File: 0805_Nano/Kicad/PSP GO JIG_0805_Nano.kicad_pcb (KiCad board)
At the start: 2 copper layers, 20.1 x 14 mm, 12 parts

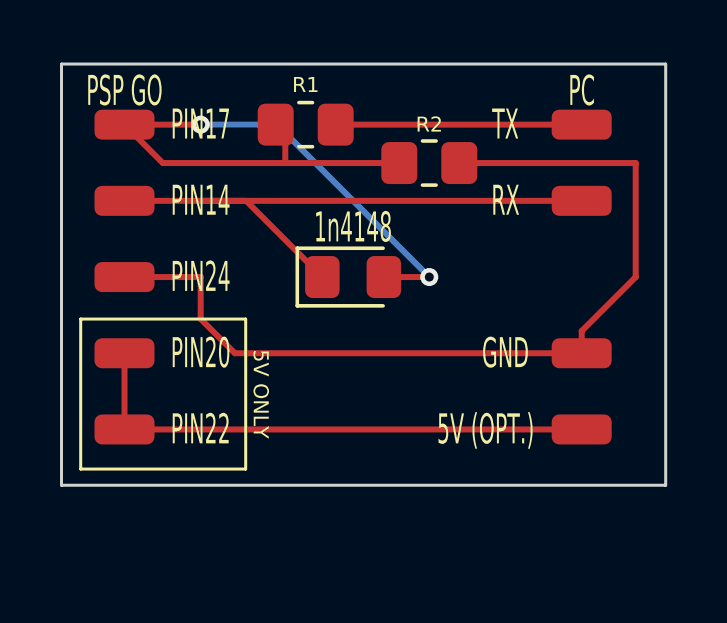
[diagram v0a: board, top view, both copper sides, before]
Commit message: fixed issues pertaining to k-line schematics
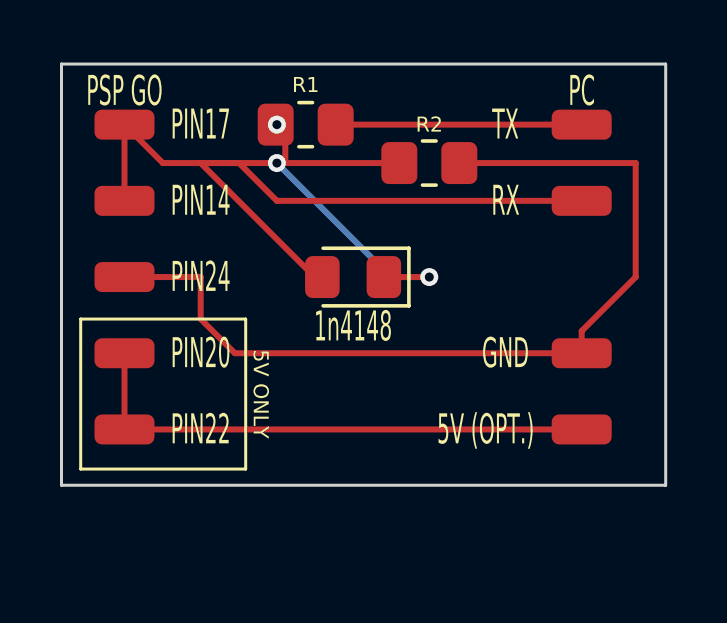
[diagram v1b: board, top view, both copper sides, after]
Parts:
- turned 1n4148 to 180 degrees
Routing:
- net (no net): track 101.3 -> 96.7 mm, vias 2 -> 3
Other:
- board text added: "PSP GO JIG 0805 Rev 1.1 by Mathieulh"
- board text removed: "PSP GO JIG 0805 Rev 1.0 by Mathieulh"
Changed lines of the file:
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@@
   )
   (footprint "Diode_SMD:D_0805_2012Metric_Pad1.15x1.40mm_HandSolder" (layer "F.Cu")
-    (at 68.58 38.1)
+    (at 68.58 38.1 180)
     (descr "Diode SMD 0805 (2012 Metric), square (rectangular) end terminal, IPC_7351 nominal, (Body size source: https://docs.google.com/spreadsheets/d/1BsfQQcO9C6DZCsRaXUlFlo91Tg2WpOkGARC1WS5S8t0/edit?usp=sharing), generated with kicad-footprint-generator")
     (tags "diode handsolder")
@@
     (fp_line (start 1 0.6) (end 1 -0.6)
       (stroke (width 0.1) (type solid)) (layer "F.Fab"))
-    (pad "1" smd roundrect (at -1.025 0) (size 1.15 1.4) (layers "F.Cu" "F.Paste" "F.Mask") (roundrect_rratio 0.217391))
-    (pad "2" smd roundrect (at 1.025 0) (size 1.15 1.4) (layers "F.Cu" "F.Paste" "F.Mask") (roundrect_rratio 0.217391))
+    (pad "1" smd roundrect (at -1.025 0 180) (size 1.15 1.4) (layers "F.Cu" "F.Paste" "F.Mask") (roundrect_rratio 0.217391))
+    (pad "2" smd roundrect (at 1.025 0 180) (size 1.15 1.4) (layers "F.Cu" "F.Paste" "F.Mask") (roundrect_rratio 0.217391))
     (model "${KICAD6_3DMODEL_DIR}/Diode_SMD.3dshapes/D_0805_2012Metric.wrl"
       (offset (xyz 0 0 0))
@@
     (effects (font (size 0.7 0.7) (thickness 0.125) bold) (justify left bottom mirror))
   )
-  (gr_text "PSP GO JIG 0805 Rev 1.0 by Mathieulh" (at 73.66 32.37) (layer "B.SilkS")
+  (gr_text "PSP GO JIG 0805 Rev 1.1 by Mathieulh" (at 73.66 32.37) (layer "B.SilkS")
     (effects (font (size 0.7 0.5) (thickness 0.1) bold) (justify left bottom mirror))
   )
@@
     (effects (font (size 1 0.5) (thickness 0.15)))
   )
-  (segment (start 66.32 33.34) (end 66 33.02) (width 0.2) (layer "F.Cu") (net 0))
+  (segment (start 66.32 34.3) (end 63.5 34.3) (width 0.2) (layer "F.Cu") (net 0))
+  (segment (start 66.32 33.34) (end 66.04 33.06) (width 0.2) (layer "F.Cu") (net 0))
   (segment (start 62.24 34.3) (end 60.96 33.02) (width 0.2) (layer "F.Cu") (net 0))
-  (segment (start 66.32 34.3) (end 62.24 34.3) (width 0.2) (layer "F.Cu") (net 0))
+  (segment (start 63.5 34.3) (end 62.24 34.3) (width 0.2) (layer "F.Cu") (net 0))
   (segment (start 60.96 38.1) (end 63.5 38.1) (width 0.2) (layer "F.Cu") (net 0))
+  (segment (start 66.04 33.02) (end 66 33.02) (width 0.2) (layer "F.Cu") (net 0))
+  (segment (start 66.04 33.06) (end 66.04 33.02) (width 0.2) (layer "F.Cu") (net 0))
   (segment (start 78 38.1) (end 76.2 39.9) (width 0.2) (layer "F.Cu") (net 0))
   (segment (start 64.64 40.64) (end 76.2 40.64) (width 0.2) (layer "F.Cu") (net 0))
-  (segment (start 60.96 33.02) (end 63.5 33.02) (width 0.2) (layer "F.Cu") (net 0))
   (segment (start 63.5 38.1) (end 63.5 39.5) (width 0.2) (layer "F.Cu") (net 0))
   (segment (start 78 34.3) (end 78 38.1) (width 0.2) (layer "F.Cu") (net 0))
+  (segment (start 60.96 33.02) (end 60.96 35.56) (width 0.2) (layer "F.Cu") (net 0))
+  (segment (start 66 33.02) (end 66 33.02) (width 0.2) (layer "F.Cu") (net 0))
   (segment (start 66.32 34.3) (end 66.32 33.34) (width 0.2) (layer "F.Cu") (net 0))
+  (segment (start 67.3 38.1) (end 63.5 34.3) (width 0.2) (layer "F.Cu") (net 0))
   (segment (start 63.5 39.5) (end 64.64 40.64) (width 0.2) (layer "F.Cu") (net 0))
   (segment (start 60.96 43.18) (end 60.96 40.64) (width 0.2) (layer "F.Cu") (net 0))
   (segment (start 70.12 34.3) (end 66.32 34.3) (width 0.2) (layer "F.Cu") (net 0))
+  (segment (start 66.04 35.56) (end 64.78 34.3) (width 0.2) (layer "F.Cu") (net 0))
+  (segment (start 67.555 38.1) (end 67.3 38.1) (width 0) (layer "F.Cu") (net 0))
+  (segment (start 64.78 34.3) (end 63.5 34.3) (width 0.2) (layer "F.Cu") (net 0))
   (segment (start 72.12 34.3) (end 78 34.3) (width 0.2) (layer "F.Cu") (net 0))
-  (segment (start 63.5 35.56) (end 76.2 35.56) (width 0.2) (layer "F.Cu") (net 0))
   (segment (start 76.2 39.9) (end 76.2 40.64) (width 0.2) (layer "F.Cu") (net 0))
+  (segment (start 66.04 35.56) (end 76.2 35.56) (width 0.2) (layer "F.Cu") (net 0))
   (segment (start 68 33.02) (end 76.2 33.02) (width 0.2) (layer "F.Cu") (net 0))
-  (segment (start 67.555 38.1) (end 65.015 35.56) (width 0.2) (layer "F.Cu") (net 0))
-  (segment (start 65.015 35.56) (end 63.5 35.56) (width 0.2) (layer "F.Cu") (net 0))
-  (segment (start 60.96 35.56) (end 63.5 35.56) (width 0.2) (layer "F.Cu") (net 0))
   (segment (start 71.12 38.1) (end 69.605 38.1) (width 0.2) (layer "F.Cu") (net 0))
   (segment (start 60.96 43.18) (end 76.2 43.18) (width 0.2) (layer "F.Cu") (net 0))
+  (via (at 66.04 33.02) (size 0.6) (drill 0.3) (layers "F.Cu" "B.Cu") (net 0))
   (via (at 71.12 38.1) (size 0.6) (drill 0.3) (layers "F.Cu" "B.Cu") (net 0))
-  (via (at 63.5 33.02) (size 0.6) (drill 0.3) (layers "F.Cu" "B.Cu") (net 0))
-  (segment (start 63.5 33.02) (end 66.04 33.02) (width 0.2) (layer "B.Cu") (net 0))
-  (segment (start 66.04 33.02) (end 71.12 38.1) (width 0.2) (layer "B.Cu") (net 0))
+  (via (at 66.04 34.3) (size 0.6) (drill 0.3) (layers "F.Cu" "B.Cu") (net 0))
+  (segment (start 69.84 38.1) (end 71.12 38.1) (width 0.2) (layer "B.Cu") (net 0))
+  (segment (start 66.04 34.3) (end 69.84 38.1) (width 0.2) (layer "B.Cu") (net 0))
 )

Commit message: Fixed PIN24
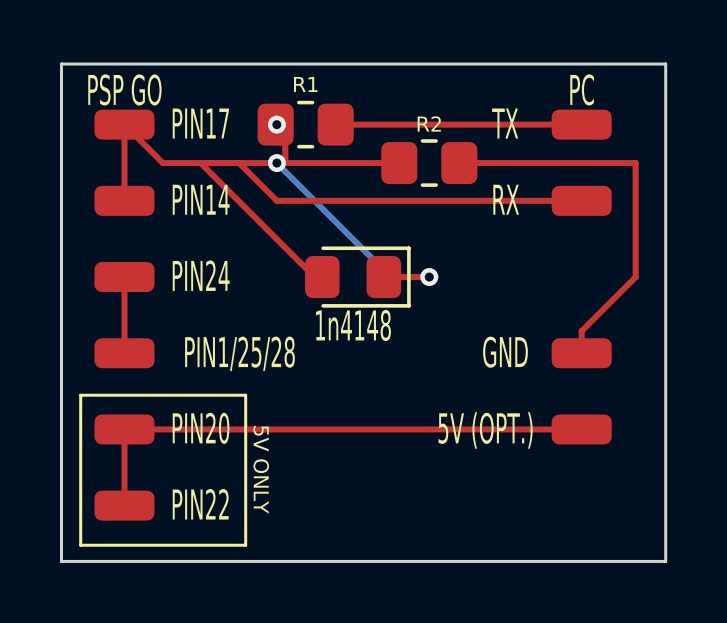
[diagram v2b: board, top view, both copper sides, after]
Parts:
- added REF**: SolderWirePad_1x01_SMD_1x2mm, Connector_Wire:SolderWirePad_1x01_SMD_1x2mm, F.Cu at (61.0, 40.6)
- moved REF** 2.54 mm to (61.0, 45.7)
- moved REF** 2.54 mm to (61.0, 43.2)
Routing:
- net (no net): track 96.7 -> 66.9 mm
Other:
- board size 20.1 x 14 mm -> 20.1 x 16.6 mm
- board text added: "PIN1/25/28"

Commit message: Cleanup + fix GND
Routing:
- net (no net): vias 3 -> 2
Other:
- board text added: "PSP GO JIG 0805 Rev 1.2 by Mathieulh"
- board text removed: "PSP GO JIG 0805 Rev 1.1 by Mathieulh"
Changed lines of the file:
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@@
   (gr_line (start 60.96 43.18) (end 76.2 43.18)
+    (stroke (width 0.2) (type default)) (layer "F.Cu"))
+  (gr_line (start 76.2 40.64) (end 60.96 40.64)
     (stroke (width 0.2) (type default)) (layer "F.Cu"))
   (gr_rect (start 69.46 36.19) (end 76.2 40.01)
@@
     (effects (font (size 0.7 0.7) (thickness 0.125) bold) (justify left bottom mirror))
   )
-  (gr_text "PSP GO JIG 0805 Rev 1.1 by Mathieulh" (at 73.66 32.37) (layer "B.SilkS")
+  (gr_text "PSP GO JIG 0805 Rev 1.2 by Mathieulh" (at 73.66 32.37) (layer "B.SilkS")
     (effects (font (size 0.7 0.5) (thickness 0.1) bold) (justify left bottom mirror))
   )
@@
   (segment (start 71.12 38.1) (end 69.605 38.1) (width 0.2) (layer "F.Cu") (net 0))
   (segment (start 60.96 38.1) (end 60.96 40.64) (width 0.2) (layer "F.Cu") (net 0))
-  (via (at 66.04 33.02) (size 0.6) (drill 0.3) (layers "F.Cu" "B.Cu") (net 0))
   (via (at 71.12 38.1) (size 0.6) (drill 0.3) (layers "F.Cu" "B.Cu") (net 0))
   (via (at 66.04 34.3) (size 0.6) (drill 0.3) (layers "F.Cu" "B.Cu") (net 0))

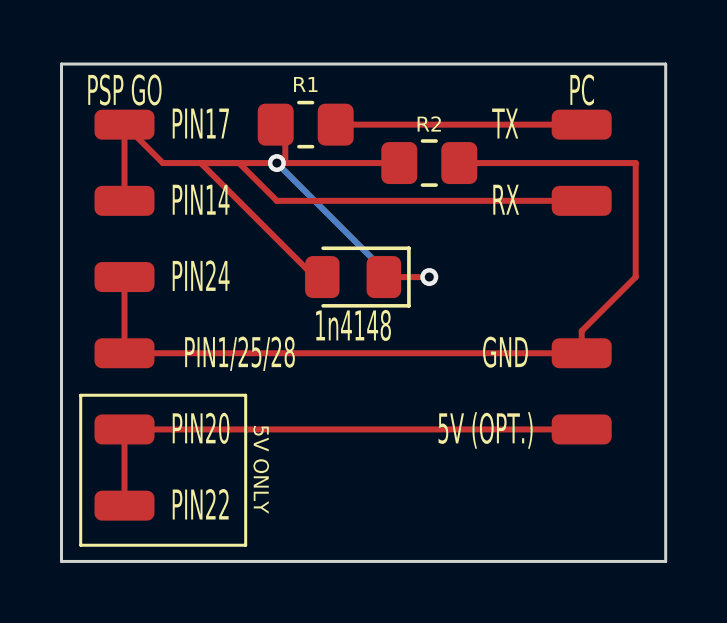
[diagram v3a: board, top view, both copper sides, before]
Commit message: Fixed design issue on nano board
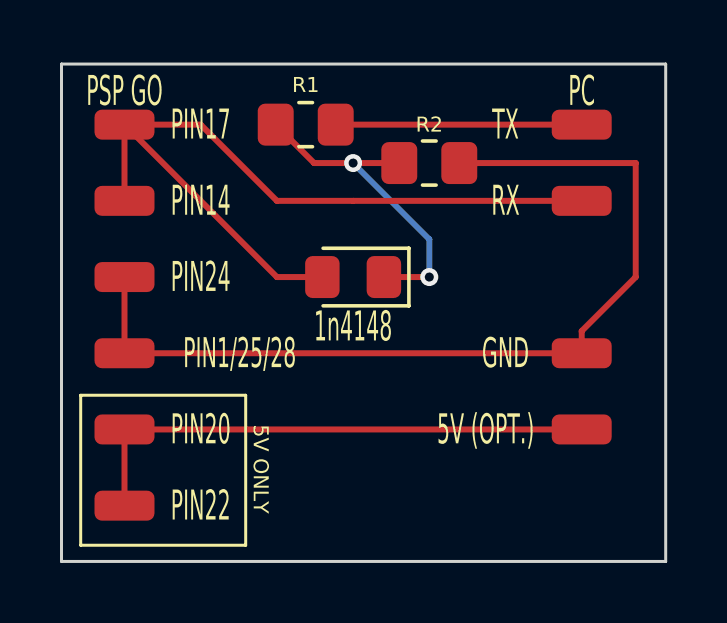
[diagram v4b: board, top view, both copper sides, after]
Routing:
- net (no net): track 66.9 -> 65.5 mm
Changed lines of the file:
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@@
     (effects (font (size 1 0.5) (thickness 0.15)))
   )
-  (segment (start 66.32 34.3) (end 63.5 34.3) (width 0.2) (layer "F.Cu") (net 0))
   (segment (start 66.32 33.34) (end 66.04 33.06) (width 0.2) (layer "F.Cu") (net 0))
-  (segment (start 62.24 34.3) (end 60.96 33.02) (width 0.2) (layer "F.Cu") (net 0))
-  (segment (start 63.5 34.3) (end 62.24 34.3) (width 0.2) (layer "F.Cu") (net 0))
+  (segment (start 66.04 35.56) (end 63.5 33.02) (width 0.2) (layer "F.Cu") (net 0))
   (segment (start 66.04 33.02) (end 66 33.02) (width 0.2) (layer "F.Cu") (net 0))
   (segment (start 66.04 33.06) (end 66.04 33.02) (width 0.2) (layer "F.Cu") (net 0))
   (segment (start 78 38.1) (end 76.2 39.9) (width 0.2) (layer "F.Cu") (net 0))
+  (segment (start 68.58 35.56) (end 76.2 35.56) (width 0.2) (layer "F.Cu") (net 0))
   (segment (start 78 34.3) (end 78 38.1) (width 0.2) (layer "F.Cu") (net 0))
   (segment (start 60.96 33.02) (end 60.96 35.56) (width 0.2) (layer "F.Cu") (net 0))
   (segment (start 66 33.02) (end 66 33.02) (width 0.2) (layer "F.Cu") (net 0))
-  (segment (start 66.32 34.3) (end 66.32 33.34) (width 0.2) (layer "F.Cu") (net 0))
-  (segment (start 67.3 38.1) (end 63.5 34.3) (width 0.2) (layer "F.Cu") (net 0))
   (segment (start 60.96 45.72) (end 60.96 43.18) (width 0.2) (layer "F.Cu") (net 0))
-  (segment (start 70.12 34.3) (end 66.32 34.3) (width 0.2) (layer "F.Cu") (net 0))
-  (segment (start 66.04 35.56) (end 64.78 34.3) (width 0.2) (layer "F.Cu") (net 0))
+  (segment (start 70.12 34.3) (end 67.28 34.3) (width 0.2) (layer "F.Cu") (net 0))
   (segment (start 67.555 38.1) (end 67.3 38.1) (width 0) (layer "F.Cu") (net 0))
-  (segment (start 64.78 34.3) (end 63.5 34.3) (width 0.2) (layer "F.Cu") (net 0))
+  (segment (start 66.04 38.1) (end 60.96 33.02) (width 0.2) (layer "F.Cu") (net 0))
   (segment (start 72.12 34.3) (end 78 34.3) (width 0.2) (layer "F.Cu") (net 0))
+  (segment (start 63.5 33.02) (end 60.96 33.02) (width 0.2) (layer "F.Cu") (net 0))
+  (segment (start 67.28 34.3) (end 66 33.02) (width 0.2) (layer "F.Cu") (net 0))
   (segment (start 76.2 39.9) (end 76.2 40.64) (width 0.2) (layer "F.Cu") (net 0))
-  (segment (start 66.04 35.56) (end 76.2 35.56) (width 0.2) (layer "F.Cu") (net 0))
+  (segment (start 66.04 35.56) (end 68.58 35.56) (width 0.2) (layer "F.Cu") (net 0))
   (segment (start 68 33.02) (end 76.2 33.02) (width 0.2) (layer "F.Cu") (net 0))
   (segment (start 71.12 38.1) (end 69.605 38.1) (width 0.2) (layer "F.Cu") (net 0))
+  (segment (start 67.555 38.1) (end 66.04 38.1) (width 0.2) (layer "F.Cu") (net 0))
   (segment (start 60.96 38.1) (end 60.96 40.64) (width 0.2) (layer "F.Cu") (net 0))
   (via (at 71.12 38.1) (size 0.6) (drill 0.3) (layers "F.Cu" "B.Cu") (net 0))
-  (via (at 66.04 34.3) (size 0.6) (drill 0.3) (layers "F.Cu" "B.Cu") (net 0))
-  (segment (start 69.84 38.1) (end 71.12 38.1) (width 0.2) (layer "B.Cu") (net 0))
-  (segment (start 66.04 34.3) (end 69.84 38.1) (width 0.2) (layer "B.Cu") (net 0))
+  (via (at 68.58 34.3) (size 0.6) (drill 0.3) (layers "F.Cu" "B.Cu") (net 0))
+  (segment (start 68.58 34.3) (end 71.12 36.84) (width 0.2) (layer "B.Cu") (net 0))
+  (segment (start 71.12 36.84) (end 71.12 38.1) (width 0.2) (layer "B.Cu") (net 0))
 )

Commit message: Fix PIN 20
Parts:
- added R3: R_0805_2012Metric_Pad1.20x1.40mm_HandSolder, Resistor_SMD:R_0805_2012Metric_Pad1.20x1.40mm_HandSolder, F.Cu at (69.0, 43.2)
- renumbered REF** to R1, REF** to R2
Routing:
- net (no net): track 65.5 -> 92.6 mm
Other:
- board text added: "10KR"
- board text added: "PSP GO JIG 0805 Rev 1.3 by Mathieulh"
- board text removed: "PSP GO JIG 0805 Rev 1.2 by Mathieulh"
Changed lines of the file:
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@@
   )
   (footprint "Resistor_SMD:R_0805_2012Metric_Pad1.20x1.40mm_HandSolder" (layer "F.Cu")
-    (at 71.12 34.3)
+    (at 69 43.18)
     (descr "Resistor SMD 0805 (2012 Metric), square (rectangular) end terminal, IPC_7351 nominal with elongated pad for handsoldering. (Body size source: IPC-SM-782 page 72, https://www.pcb-3d.com/wordpress/wp-content/uploads/ipc-sm-782a_amendment_1_and_2.pdf), generated with kicad-footprint-generator")
     (tags "resistor handsolder")
     (attr smd)
-    (fp_text reference "REF**" (at 0 -1.65) (layer "F.SilkS") hide
+    (fp_text reference "R3" (at 0 -1.65) (layer "F.SilkS") hide
         (effects (font (size 1 1) (thickness 0.15)))
     )
@@
   )
   (footprint "Resistor_SMD:R_0805_2012Metric_Pad1.20x1.40mm_HandSolder" (layer "F.Cu")
+    (at 71.12 34.3)
+    (descr "Resistor SMD 0805 (2012 Metric), square (rectangular) end terminal, IPC_7351 nominal with elongated pad for handsoldering. (Body size source: IPC-SM-782 page 72, https://www.pcb-3d.com/wordpress/wp-content/uploads/ipc-sm-782a_amendment_1_and_2.pdf), generated with kicad-footprint-generator")
+    (tags "resistor handsolder")
+    (attr smd)
+    (fp_text reference "R2" (at 0 -1.65) (layer "F.SilkS") hide
+        (effects (font (size 1 1) (thickness 0.15)))
+    )
+    (fp_text value "R_0805_2012Metric_Pad1.20x1.40mm_HandSolder" (at 0 1.65) (layer "F.Fab")
+        (effects (font (size 1 1) (thickness 0.15)))
+    )
+    (fp_text user "${REFERENCE}" (at 0 0) (layer "F.Fab")
+        (effects (font (size 0.5 0.5) (thickness 0.08)))
+    )
+    (fp_line (start -0.227064 -0.735) (end 0.227064 -0.735)
+      (stroke (width 0.12) (type solid)) (layer "F.SilkS"))
+    (fp_line (start -0.227064 0.735) (end 0.227064 0.735)
+      (stroke (width 0.12) (type solid)) (layer "F.SilkS"))
+    (fp_line (start -1.85 -0.95) (end 1.85 -0.95)
+      (stroke (width 0.05) (type solid)) (layer "F.CrtYd"))
+    (fp_line (start -1.85 0.95) (end -1.85 -0.95)
+      (stroke (width 0.05) (type solid)) (layer "F.CrtYd"))
+    (fp_line (start 1.85 -0.95) (end 1.85 0.95)
+      (stroke (width 0.05) (type solid)) (layer "F.CrtYd"))
+    (fp_line (start 1.85 0.95) (end -1.85 0.95)
+      (stroke (width 0.05) (type solid)) (layer "F.CrtYd"))
+    (fp_line (start -1 -0.625) (end 1 -0.625)
+      (stroke (width 0.1) (type solid)) (layer "F.Fab"))
+    (fp_line (start -1 0.625) (end -1 -0.625)
+      (stroke (width 0.1) (type solid)) (layer "F.Fab"))
+    (fp_line (start 1 -0.625) (end 1 0.625)
+      (stroke (width 0.1) (type solid)) (layer "F.Fab"))
+    (fp_line (start 1 0.625) (end -1 0.625)
+      (stroke (width 0.1) (type solid)) (layer "F.Fab"))
+    (pad "1" smd roundrect (at -1 0) (size 1.2 1.4) (layers "F.Cu" "F.Paste" "F.Mask") (roundrect_rratio 0.2083333333))
+    (pad "2" smd roundrect (at 1 0) (size 1.2 1.4) (layers "F.Cu" "F.Paste" "F.Mask") (roundrect_rratio 0.2083333333))
+    (model "${KICAD6_3DMODEL_DIR}/Resistor_SMD.3dshapes/R_0805_2012Metric.wrl"
+      (offset (xyz 0 0 0))
+      (scale (xyz 1 1 1))
+      (rotate (xyz 0 0 0))
+    )
+  )
+  (footprint "Resistor_SMD:R_0805_2012Metric_Pad1.20x1.40mm_HandSolder" (layer "F.Cu")
     (at 67 33.02)
     (descr "Resistor SMD 0805 (2012 Metric), square (rectangular) end terminal, IPC_7351 nominal with elongated pad for handsoldering. (Body size source: IPC-SM-782 page 72, https://www.pcb-3d.com/wordpress/wp-content/uploads/ipc-sm-782a_amendment_1_and_2.pdf), generated with kicad-footprint-generator")
     (tags "resistor handsolder")
     (attr smd)
-    (fp_text reference "REF**" (at 0 -1.65) (layer "F.SilkS") hide
+    (fp_text reference "R1" (at 0 -1.65) (layer "F.SilkS") hide
         (effects (font (size 1 1) (thickness 0.15)))
     )
@@
     (pad "4" smd roundrect (at 0 0 270) (size 1 2) (layers "F.Cu" "F.Paste" "F.Mask") (roundrect_rratio 0.25))
   )
-  (gr_line (start 60.96 43.18) (end 76.2 43.18)
-    (stroke (width 0.2) (type default)) (layer "F.Cu"))
   (gr_line (start 76.2 40.64) (end 60.96 40.64)
     (stroke (width 0.2) (type default)) (layer "F.Cu"))
@@
     (effects (font (size 0.7 0.7) (thickness 0.125) bold) (justify left bottom mirror))
   )
-  (gr_text "PSP GO JIG 0805 Rev 1.2 by Mathieulh" (at 73.66 32.37) (layer "B.SilkS")
+  (gr_text "PSP GO JIG 0805 Rev 1.3 by Mathieulh" (at 73.66 32.37) (layer "B.SilkS")
     (effects (font (size 0.7 0.5) (thickness 0.1) bold) (justify left bottom mirror))
   )
   (gr_text "3.3V\nR1=1K\nR2=1K\n" (at 76.2 40.01) (layer "B.SilkS")
     (effects (font (size 0.7 0.7) (thickness 0.125) bold) (justify left bottom mirror))
+  )
+  (gr_text "10KR" (at 69 41.89) (layer "F.SilkS")
+    (effects (font (size 0.5 0.5) (thickness 0.125)))
   )
   (gr_text "5V ONLY" (at 65.5 44.5 270) (layer "F.SilkS")
@@
   (segment (start 78 38.1) (end 76.2 39.9) (width 0.2) (layer "F.Cu") (net 0))
   (segment (start 68.58 35.56) (end 76.2 35.56) (width 0.2) (layer "F.Cu") (net 0))
+  (segment (start 74.084264 45.72) (end 76.412132 43.392132) (width 0.2) (layer "F.Cu") (net 0))
   (segment (start 78 34.3) (end 78 38.1) (width 0.2) (layer "F.Cu") (net 0))
   (segment (start 60.96 33.02) (end 60.96 35.56) (width 0.2) (layer "F.Cu") (net 0))
+  (segment (start 60.96 43.18) (end 68 43.18) (width 0.2) (layer "F.Cu") (net 0))
   (segment (start 66 33.02) (end 66 33.02) (width 0.2) (layer "F.Cu") (net 0))
-  (segment (start 60.96 45.72) (end 60.96 43.18) (width 0.2) (layer "F.Cu") (net 0))
   (segment (start 70.12 34.3) (end 67.28 34.3) (width 0.2) (layer "F.Cu") (net 0))
   (segment (start 67.555 38.1) (end 67.3 38.1) (width 0) (layer "F.Cu") (net 0))
@@
   (segment (start 76.2 39.9) (end 76.2 40.64) (width 0.2) (layer "F.Cu") (net 0))
   (segment (start 66.04 35.56) (end 68.58 35.56) (width 0.2) (layer "F.Cu") (net 0))
+  (segment (start 60.96 45.72) (end 74.084264 45.72) (width 0.2) (layer "F.Cu") (net 0))
   (segment (start 68 33.02) (end 76.2 33.02) (width 0.2) (layer "F.Cu") (net 0))
+  (segment (start 70 43.18) (end 76.2 43.18) (width 0.2) (layer "F.Cu") (net 0))
   (segment (start 71.12 38.1) (end 69.605 38.1) (width 0.2) (layer "F.Cu") (net 0))
   (segment (start 67.555 38.1) (end 66.04 38.1) (width 0.2) (layer "F.Cu") (net 0))
